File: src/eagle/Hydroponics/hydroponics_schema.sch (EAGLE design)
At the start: 16 parts, among them U1 ULN2003A, U2 DS1307Z+

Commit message: add eagle schema
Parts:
- C1, G1, JP1, JP2, JP3, JP4, R1, R2, R3, R4: OC_NEWARK (none) -> unknown
- U1: MF (none) -> Arrow Electronics
- U2: MF (none) -> DALLAS SEMICONDUCTOR
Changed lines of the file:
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@@
 </classes>
 <parts>
-<part name="JP1" library="pinhead" deviceset="PINHD-1X8" device="/90"/>
-<part name="JP2" library="pinhead" deviceset="PINHD-1X8" device="/90"/>
-<part name="JP3" library="pinhead" deviceset="PINHD-1X6" device="/90"/>
-<part name="JP4" library="pinhead" deviceset="PINHD-1X6" device="/90"/>
+<part name="JP1" library="pinhead" deviceset="PINHD-1X8" device="/90">
+<attribute name="MF" value=""/>
+<attribute name="MPN" value=""/>
+<attribute name="OC_NEWARK" value="unknown"/>
+</part>
+<part name="JP2" library="pinhead" deviceset="PINHD-1X8" device="/90">
+<attribute name="MF" value=""/>
+<attribute name="MPN" value=""/>
+<attribute name="OC_NEWARK" value="unknown"/>
+</part>
+<part name="JP3" library="pinhead" deviceset="PINHD-1X6" device="/90">
+<attribute name="MF" value=""/>
+<attribute name="MPN" value=""/>
+<attribute name="OC_NEWARK" value="unknown"/>
+</part>
+<part name="JP4" library="pinhead" deviceset="PINHD-1X6" device="/90">
+<attribute name="MF" value=""/>
+<attribute name="MPN" value=""/>
+<attribute name="OC_NEWARK" value="unknown"/>
+</part>
 <part name="SV1" library="con-lsta" deviceset="FE07-1" device=""/>
-<part name="U1" library="ST Microelctronics_By_element14_Batch_1" deviceset="ULN2003A" device=""/>
-<part name="U2" library="Maxim_By_element14_Batch_1" deviceset="DS1307Z+" device=""/>
+<part name="U1" library="ST Microelctronics_By_element14_Batch_1" deviceset="ULN2003A" device="">
+<attribute name="MF" value="Arrow Electronics"/>
+</part>
+<part name="U2" library="Maxim_By_element14_Batch_1" deviceset="DS1307Z+" device="">
+<attribute name="MF" value="DALLAS SEMICONDUCTOR"/>
+</part>
 <part name="Q1" library="crystal" deviceset="CRYSTAL" device="TC38H"/>
 <part name="SV2" library="con-lsta" deviceset="FE08-1" device=""/>
-<part name="R1" library="resistor" deviceset="R-EU_" device="0207/10"/>
-<part name="R2" library="resistor" deviceset="R-EU_" device="0207/10"/>
-<part name="R3" library="resistor" deviceset="R-EU_" device="0207/10"/>
-<part name="R4" library="resistor" deviceset="R-EU_" device="0207/10"/>
-<part name="C1" library="rcl" deviceset="C-EU" device="025-025X050"/>
-<part name="G1" library="battery" deviceset="CR2032H" device=""/>
+<part name="R1" library="resistor" deviceset="R-EU_" device="0207/10">
+<attribute name="MF" value=""/>
+<attribute name="MPN" value=""/>
+<attribute name="OC_NEWARK" value="unknown"/>
+</part>
+<part name="R2" library="resistor" deviceset="R-EU_" device="0207/10">
+<attribute name="MF" value=""/>
+<attribute name="MPN" value=""/>
+<attribute name="OC_NEWARK" value="unknown"/>
+</part>
+<part name="R3" library="resistor" deviceset="R-EU_" device="0207/10">
+<attribute name="MF" value=""/>
+<attribute name="MPN" value=""/>
+<attribute name="OC_NEWARK" value="unknown"/>
+</part>
+<part name="R4" library="resistor" deviceset="R-EU_" device="0207/10">
+<attribute name="MF" value=""/>
+<attribute name="MPN" value=""/>
+<attribute name="OC_NEWARK" value="unknown"/>
+</part>
+<part name="C1" library="rcl" deviceset="C-EU" device="025-025X050">
+<attribute name="MF" value=""/>
+<attribute name="MPN" value=""/>
+<attribute name="OC_NEWARK" value="unknown"/>
+</part>
+<part name="G1" library="battery" deviceset="CR2032H" device="">
+<attribute name="MF" value=""/>
+<attribute name="MPN" value=""/>
+<attribute name="OC_NEWARK" value="unknown"/>
+</part>
 <part name="SV3" library="con-lsta" deviceset="FE05-1" device=""/>
 </parts>
@@
 </plain>
 <instances>
-<instance part="JP1" gate="A" x="-66.04" y="144.78" rot="R90"/>
-<instance part="JP2" gate="A" x="-33.02" y="144.78" rot="R90"/>
-<instance part="JP3" gate="A" x="-78.74" y="27.94" rot="R270"/>
-<instance part="JP4" gate="A" x="-50.8" y="27.94" rot="R270"/>
+<instance part="JP1" gate="A" x="-66.04" y="144.78" rot="R90">
+<attribute name="OC_NEWARK" x="-66.04" y="144.78" size="1.778" layer="96" display="off"/>
+<attribute name="MF" x="-66.04" y="144.78" size="1.778" layer="96" display="off"/>
+<attribute name="MPN" x="-66.04" y="144.78" size="1.778" layer="96" display="off"/>
+</instance>
+<instance part="JP2" gate="A" x="-33.02" y="144.78" rot="R90">
+<attribute name="OC_NEWARK" x="-33.02" y="144.78" size="1.778" layer="96" display="off"/>
+<attribute name="MF" x="-33.02" y="144.78" size="1.778" layer="96" display="off"/>
+<attribute name="MPN" x="-33.02" y="144.78" size="1.778" layer="96" display="off"/>
+</instance>
+<instance part="JP3" gate="A" x="-78.74" y="27.94" rot="R270">
+<attribute name="OC_NEWARK" x="-78.74" y="27.94" size="1.778" layer="96" display="off"/>
+<attribute name="MF" x="-78.74" y="27.94" size="1.778" layer="96" display="off"/>
+<attribute name="MPN" x="-78.74" y="27.94" size="1.778" layer="96" display="off"/>
+</instance>
+<instance part="JP4" gate="A" x="-50.8" y="27.94" rot="R270">
+<attribute name="OC_NEWARK" x="-50.8" y="27.94" size="1.778" layer="96" display="off"/>
+<attribute name="MF" x="-50.8" y="27.94" size="1.778" layer="96" display="off"/>
+<attribute name="MPN" x="-50.8" y="27.94" size="1.778" layer="96" display="off"/>
+</instance>
 <instance part="SV1" gate="G$1" x="73.66" y="96.52" rot="R180"/>
-<instance part="U1" gate="A" x="20.32" y="96.52"/>
-<instance part="U2" gate="A" x="-91.44" y="93.98"/>
+<instance part="U1" gate="A" x="20.32" y="96.52">
+<attribute name="MF" x="20.32" y="96.52" size="1.778" layer="96" display="off"/>
+</instance>
+<instance part="U2" gate="A" x="-91.44" y="93.98">
+<attribute name="MF" x="-91.44" y="93.98" size="1.778" layer="96" display="off"/>
+</instance>
 <instance part="Q1" gate="G$1" x="-91.44" y="111.76"/>
 <instance part="SV2" gate="G$1" x="73.66" y="55.88" rot="R180"/>
-<instance part="R1" gate="G$1" x="-53.34" y="48.26"/>
-<instance part="R2" gate="G$1" x="-66.04" y="38.1"/>
-<instance part="R3" gate="G$1" x="-66.04" y="40.64"/>
-<instance part="R4" gate="G$1" x="-63.5" y="58.42"/>
-<instance part="C1" gate="G$1" x="-66.04" y="45.72" rot="R90"/>
-<instance part="G1" gate="1" x="-93.98" y="63.5" rot="R180"/>
+<instance part="R1" gate="G$1" x="-53.34" y="48.26">
+<attribute name="OC_NEWARK" x="-53.34" y="48.26" size="1.778" layer="96" display="off"/>
+<attribute name="MF" x="-53.34" y="48.26" size="1.778" layer="96" display="off"/>
+<attribute name="MPN" x="-53.34" y="48.26" size="1.778" layer="96" display="off"/>
+</instance>
+<instance part="R2" gate="G$1" x="-66.04" y="38.1">
+<attribute name="OC_NEWARK" x="-66.04" y="38.1" size="1.778" layer="96" display="off"/>
+<attribute name="MF" x="-66.04" y="38.1" size="1.778" layer="96" display="off"/>
+<attribute name="MPN" x="-66.04" y="38.1" size="1.778" layer="96" display="off"/>
+</instance>
+<instance part="R3" gate="G$1" x="-66.04" y="40.64">
+<attribute name="OC_NEWARK" x="-66.04" y="40.64" size="1.778" layer="96" display="off"/>
+<attribute name="MF" x="-66.04" y="40.64" size="1.778" layer="96" display="off"/>
+<attribute name="MPN" x="-66.04" y="40.64" size="1.778" layer="96" display="off"/>
+</instance>
+<instance part="R4" gate="G$1" x="-63.5" y="58.42">
+<attribute name="OC_NEWARK" x="-63.5" y="58.42" size="1.778" layer="96" display="off"/>
+<attribute name="MF" x="-63.5" y="58.42" size="1.778" layer="96" display="off"/>
+<attribute name="MPN" x="-63.5" y="58.42" size="1.778" layer="96" display="off"/>
+</instance>
+<instance part="C1" gate="G$1" x="-66.04" y="45.72" rot="R90">
+<attribute name="OC_NEWARK" x="-66.04" y="45.72" size="1.778" layer="96" display="off"/>
+<attribute name="MF" x="-66.04" y="45.72" size="1.778" layer="96" display="off"/>
+<attribute name="MPN" x="-66.04" y="45.72" size="1.778" layer="96" display="off"/>
+</instance>
+<instance part="G1" gate="1" x="-93.98" y="63.5" rot="R180">
+<attribute name="OC_NEWARK" x="-93.98" y="63.5" size="1.778" layer="96" display="off"/>
+<attribute name="MF" x="-93.98" y="63.5" size="1.778" layer="96" display="off"/>
+<attribute name="MPN" x="-93.98" y="63.5" size="1.778" layer="96" display="off"/>
+</instance>
 <instance part="SV3" gate="G$1" x="-149.86" y="129.54"/>
 </instances>

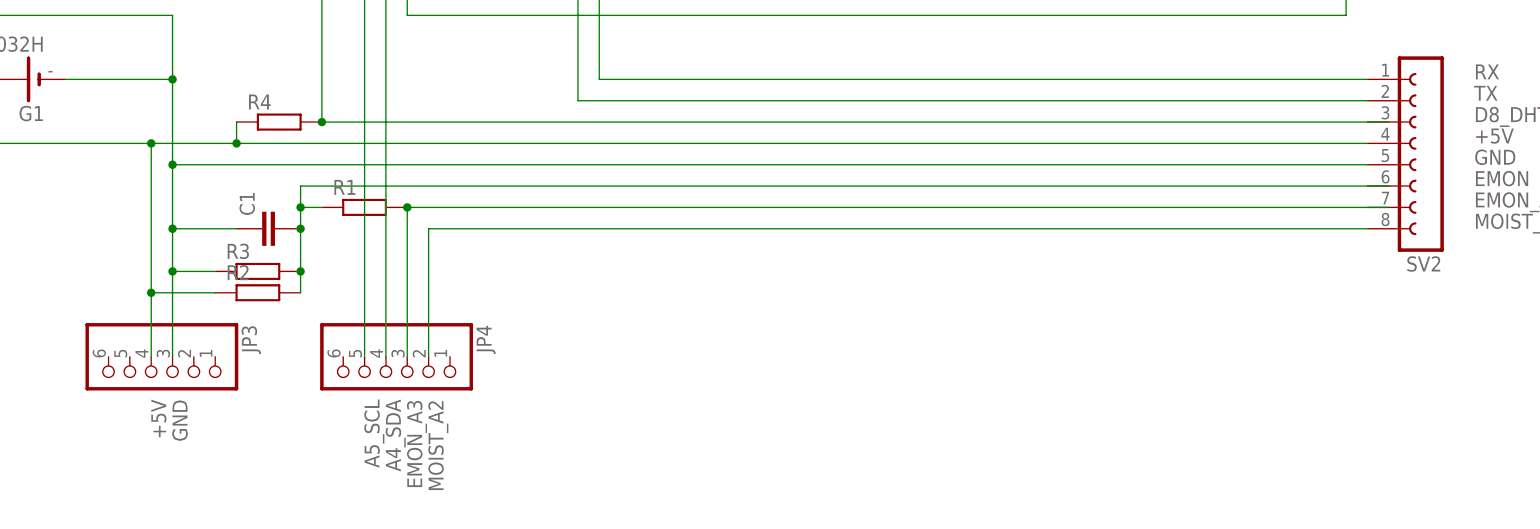
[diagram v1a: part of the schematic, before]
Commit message: change dht schema
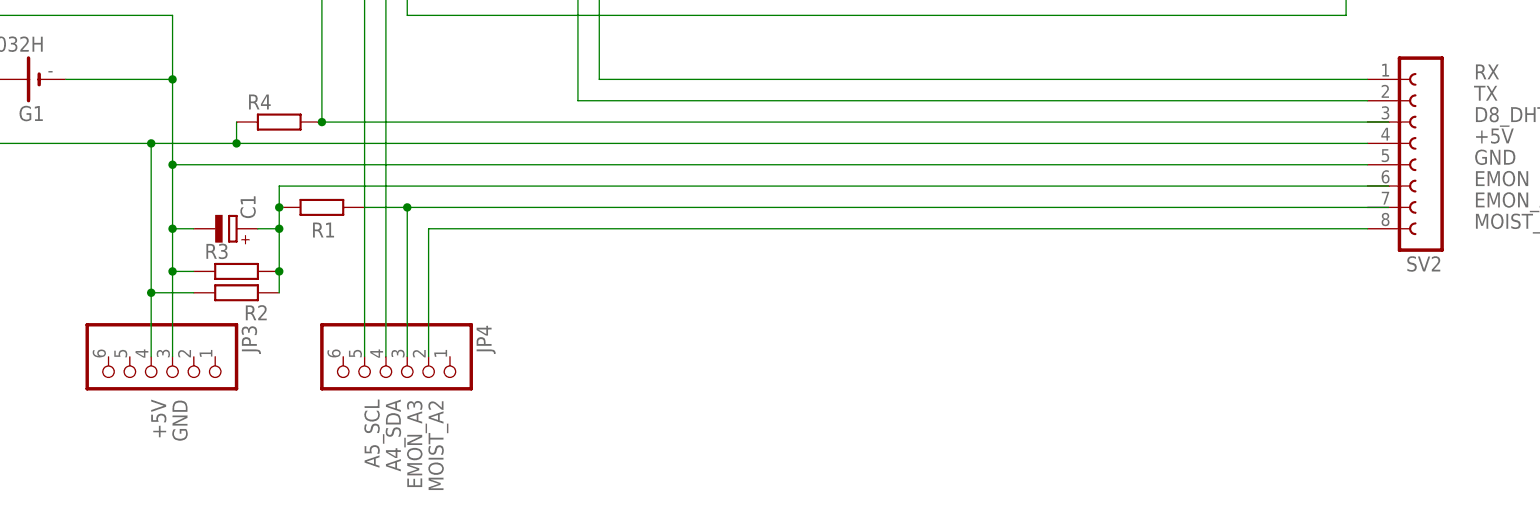
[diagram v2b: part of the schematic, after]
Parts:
- C1: device rcl:C-EU025-025X050 -> rcl:CPOL-EUE2.5-6
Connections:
- net EMON: now also C1.+; no longer C1.2
- net GND: now also C1.-; no longer C1.1
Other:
- moved on the sheet: R1, R2, R3
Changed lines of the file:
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@@
 <attribute name="OC_NEWARK" value="unknown"/>
 </part>
-<part name="C1" library="rcl" deviceset="C-EU" device="025-025X050">
+<part name="C1" library="rcl" deviceset="CPOL-EU" device="E2.5-6">
 <attribute name="MF" value=""/>
 <attribute name="MPN" value=""/>
@@
 <instance part="Q1" gate="G$1" x="-91.44" y="111.76"/>
 <instance part="SV2" gate="G$1" x="73.66" y="55.88" rot="R180"/>
-<instance part="R1" gate="G$1" x="-53.34" y="48.26">
-<attribute name="OC_NEWARK" x="-53.34" y="48.26" size="1.778" layer="96" display="off"/>
-<attribute name="MF" x="-53.34" y="48.26" size="1.778" layer="96" display="off"/>
-<attribute name="MPN" x="-53.34" y="48.26" size="1.778" layer="96" display="off"/>
-</instance>
-<instance part="R2" gate="G$1" x="-66.04" y="38.1">
-<attribute name="OC_NEWARK" x="-66.04" y="38.1" size="1.778" layer="96" display="off"/>
-<attribute name="MF" x="-66.04" y="38.1" size="1.778" layer="96" display="off"/>
-<attribute name="MPN" x="-66.04" y="38.1" size="1.778" layer="96" display="off"/>
-</instance>
-<instance part="R3" gate="G$1" x="-66.04" y="40.64">
-<attribute name="OC_NEWARK" x="-66.04" y="40.64" size="1.778" layer="96" display="off"/>
-<attribute name="MF" x="-66.04" y="40.64" size="1.778" layer="96" display="off"/>
-<attribute name="MPN" x="-66.04" y="40.64" size="1.778" layer="96" display="off"/>
+<instance part="R1" gate="G$1" x="-58.42" y="48.26" smashed="yes">
+<attribute name="OC_NEWARK" x="-58.42" y="48.26" size="1.778" layer="96" display="off"/>
+<attribute name="MF" x="-58.42" y="48.26" size="1.778" layer="96" display="off"/>
+<attribute name="MPN" x="-58.42" y="48.26" size="1.778" layer="96" display="off"/>
+<attribute name="NAME" x="-59.69" y="44.6786" size="1.778" layer="95"/>
+<attribute name="VALUE" x="-62.23" y="44.958" size="1.778" layer="96"/>
+</instance>
+<instance part="R2" gate="G$1" x="-68.58" y="38.1" smashed="yes">
+<attribute name="OC_NEWARK" x="-68.58" y="38.1" size="1.778" layer="96" display="off"/>
+<attribute name="MF" x="-68.58" y="38.1" size="1.778" layer="96" display="off"/>
+<attribute name="MPN" x="-68.58" y="38.1" size="1.778" layer="96" display="off"/>
+<attribute name="NAME" x="-64.77" y="36.6014" size="1.778" layer="95" rot="R180"/>
+<attribute name="VALUE" x="-72.39" y="34.798" size="1.778" layer="96"/>
+</instance>
+<instance part="R3" gate="G$1" x="-68.58" y="40.64" smashed="yes">
+<attribute name="OC_NEWARK" x="-68.58" y="40.64" size="1.778" layer="96" display="off"/>
+<attribute name="MF" x="-68.58" y="40.64" size="1.778" layer="96" display="off"/>
+<attribute name="MPN" x="-68.58" y="40.64" size="1.778" layer="96" display="off"/>
+<attribute name="NAME" x="-72.39" y="42.1386" size="1.778" layer="95"/>
+<attribute name="VALUE" x="-72.39" y="37.338" size="1.778" layer="96"/>
 </instance>
 <instance part="R4" gate="G$1" x="-63.5" y="58.42">
@@
 <attribute name="MPN" x="-63.5" y="58.42" size="1.778" layer="96" display="off"/>
 </instance>
-<instance part="C1" gate="G$1" x="-66.04" y="45.72" rot="R90">
-<attribute name="OC_NEWARK" x="-66.04" y="45.72" size="1.778" layer="96" display="off"/>
-<attribute name="MF" x="-66.04" y="45.72" size="1.778" layer="96" display="off"/>
-<attribute name="MPN" x="-66.04" y="45.72" size="1.778" layer="96" display="off"/>
+<instance part="C1" gate="G$1" x="-68.58" y="45.72" rot="MR90">
+<attribute name="OC_NEWARK" x="-68.58" y="45.72" size="1.778" layer="96" rot="MR0" display="off"/>
+<attribute name="MF" x="-68.58" y="45.72" size="1.778" layer="96" rot="MR0" display="off"/>
+<attribute name="MPN" x="-68.58" y="45.72" size="1.778" layer="96" rot="MR0" display="off"/>
 </instance>
 <instance part="G1" gate="1" x="-93.98" y="63.5" rot="R180">
@@
 <pinref part="R2" gate="G$1" pin="1"/>
 <wire x1="-68.58" y1="55.88" x2="66.04" y2="55.88" width="0.1524" layer="91"/>
-<wire x1="-71.12" y1="38.1" x2="-78.74" y2="38.1" width="0.1524" layer="91"/>
+<wire x1="-73.66" y1="38.1" x2="-78.74" y2="38.1" width="0.1524" layer="91"/>
 <pinref part="R4" gate="G$1" pin="1"/>
 <wire x1="-68.58" y1="58.42" x2="-68.58" y2="55.88" width="0.1524" layer="91"/>
@@
 <label x="78.74" y="53.34" size="1.778" layer="95"/>
 <pinref part="R3" gate="G$1" pin="1"/>
-<wire x1="-71.12" y1="40.64" x2="-76.2" y2="40.64" width="0.1524" layer="91"/>
+<wire x1="-73.66" y1="40.64" x2="-76.2" y2="40.64" width="0.1524" layer="91"/>
 <junction x="-76.2" y="40.64"/>
-<pinref part="C1" gate="G$1" pin="1"/>
-<wire x1="-68.58" y1="45.72" x2="-76.2" y2="45.72" width="0.1524" layer="91"/>
-<junction x="-76.2" y="45.72"/>
 <pinref part="G1" gate="1" pin="-"/>
 <wire x1="-76.2" y1="53.34" x2="-76.2" y2="63.5" width="0.1524" layer="91"/>
@@
 <wire x1="-111.76" y1="83.82" x2="-106.68" y2="83.82" width="0.1524" layer="91"/>
 <junction x="-76.2" y="63.5"/>
+<pinref part="C1" gate="G$1" pin="-"/>
+<wire x1="-73.66" y1="45.72" x2="-76.2" y2="45.72" width="0.1524" layer="91"/>
+<junction x="-76.2" y="45.72"/>
 </segment>
 </net>
@@
 <net name="EMON_A3" class="0">
 <segment>
-<pinref part="JP4" gate="A" pin="3"/>
 <wire x1="68.58" y1="48.26" x2="-48.26" y2="48.26" width="0.1524" layer="91"/>
-<wire x1="-48.26" y1="48.26" x2="-48.26" y2="30.48" width="0.1524" layer="91"/>
 <label x="-48.26" y="25.4" size="1.778" layer="95" rot="R270"/>
 <label x="78.74" y="48.26" size="1.778" layer="95"/>
 <pinref part="R1" gate="G$1" pin="2"/>
+<pinref part="JP4" gate="A" pin="3"/>
+<wire x1="-48.26" y1="48.26" x2="-53.34" y2="48.26" width="0.1524" layer="91"/>
+<wire x1="-48.26" y1="30.48" x2="-48.26" y2="48.26" width="0.1524" layer="91"/>
 <junction x="-48.26" y="48.26"/>
 </segment>
@@
 <net name="EMON" class="0">
 <segment>
+<wire x1="68.58" y1="50.8" x2="-63.5" y2="50.8" width="0.1524" layer="91"/>
+<label x="78.74" y="50.8" size="1.778" layer="95"/>
 <pinref part="R2" gate="G$1" pin="2"/>
-<wire x1="68.58" y1="50.8" x2="-60.96" y2="50.8" width="0.1524" layer="91"/>
-<wire x1="-60.96" y1="50.8" x2="-60.96" y2="48.26" width="0.1524" layer="91"/>
 <pinref part="R3" gate="G$1" pin="2"/>
-<junction x="-60.96" y="40.64"/>
-<wire x1="-60.96" y1="48.26" x2="-60.96" y2="45.72" width="0.1524" layer="91"/>
-<wire x1="-60.96" y1="45.72" x2="-60.96" y2="40.64" width="0.1524" layer="91"/>
-<wire x1="-60.96" y1="40.64" x2="-60.96" y2="38.1" width="0.1524" layer="91"/>
+<wire x1="-63.5" y1="40.64" x2="-63.5" y2="38.1" width="0.1524" layer="91"/>
+<wire x1="-63.5" y1="50.8" x2="-63.5" y2="48.26" width="0.1524" layer="91"/>
+<pinref part="C1" gate="G$1" pin="+"/>
+<wire x1="-63.5" y1="48.26" x2="-63.5" y2="45.72" width="0.1524" layer="91"/>
+<wire x1="-63.5" y1="45.72" x2="-63.5" y2="40.64" width="0.1524" layer="91"/>
+<wire x1="-66.04" y1="45.72" x2="-63.5" y2="45.72" width="0.1524" layer="91"/>
+<junction x="-63.5" y="45.72"/>
 <pinref part="R1" gate="G$1" pin="1"/>
-<wire x1="-58.42" y1="48.26" x2="-60.96" y2="48.26" width="0.1524" layer="91"/>
-<junction x="-60.96" y="48.26"/>
-<pinref part="C1" gate="G$1" pin="2"/>
-<junction x="-60.96" y="45.72"/>
-<label x="78.74" y="50.8" size="1.778" layer="95"/>
-</segment>
-</net>
+<junction x="-63.5" y="48.26"/>
+<junction x="-63.5" y="40.64"/>
+</segment>
+</net>
